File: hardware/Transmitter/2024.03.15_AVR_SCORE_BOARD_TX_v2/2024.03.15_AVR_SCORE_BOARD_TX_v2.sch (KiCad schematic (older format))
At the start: 44 parts, among them J1 Conn_01x10, J2 Conn_01x10, J3 Conn_01x05, Q1 BC817, SW1 SW_D1S+, SW10 D2S-, SW11 D2P+, SW12 D2P-, SW2 D1S-, SW3 SW_D1P+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

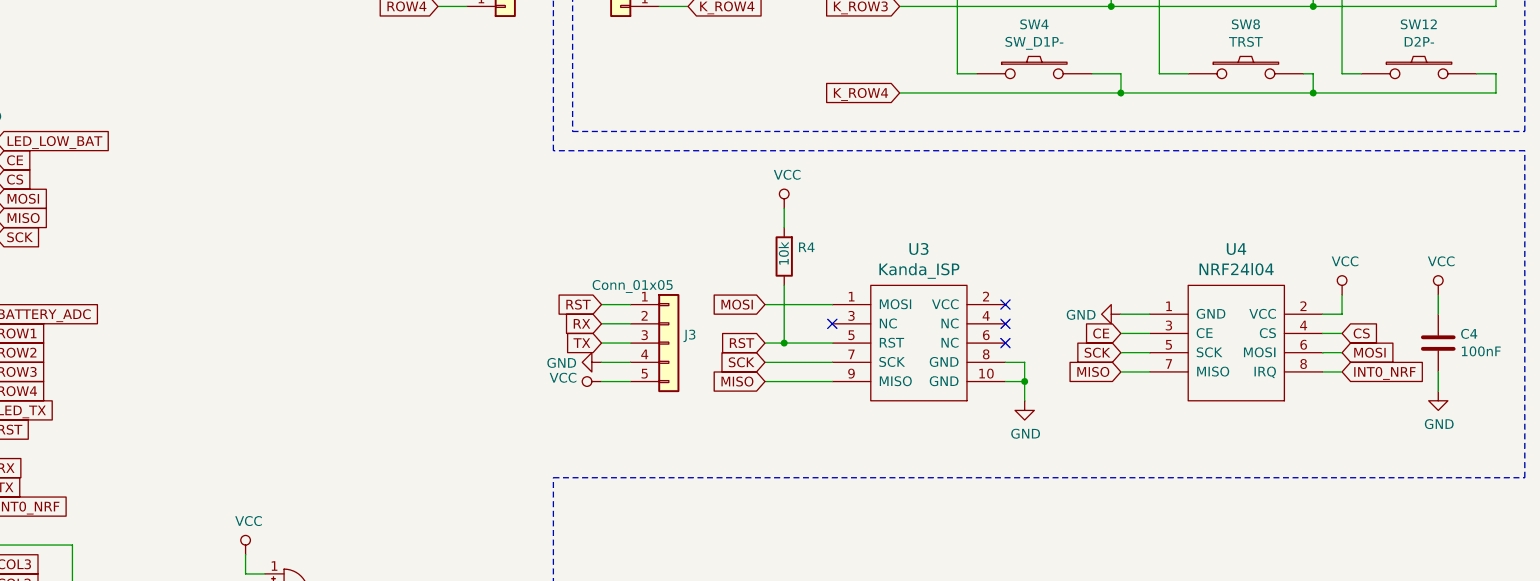
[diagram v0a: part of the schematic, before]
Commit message: Added LP2980 voltage regulator for NRF24L01
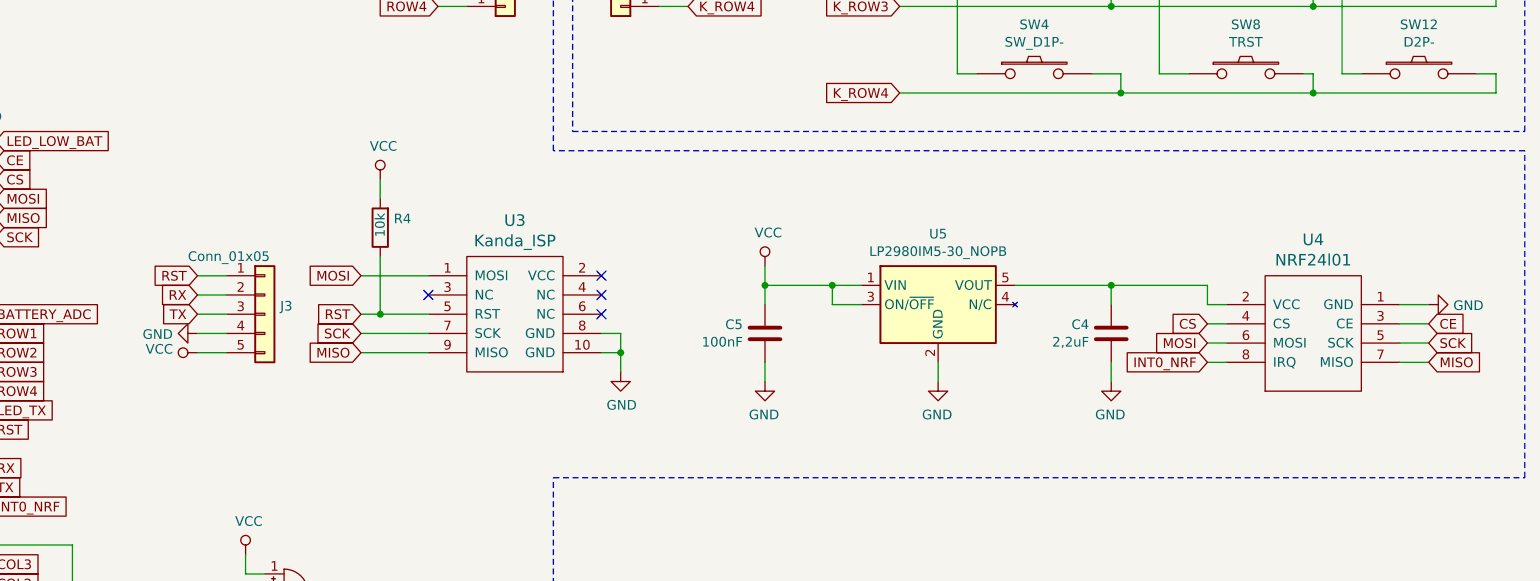
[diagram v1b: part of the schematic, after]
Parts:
- removed U4: NRF24l04, Moje:NRF24l01, symbol Moje:NRF24l04
- added C5: 100nF, Capacitor_SMD:C_0805_2012Metric_Pad1.15x1.40mm_HandSolder, symbol Device:C
- added U4: NRF24l01, Moje:NRF24l01, symbol Moje:NRF24l01
- added U5: LP2980IM5-30_NOPB, Package_TO_SOT_SMD:SOT-23-5, symbol Moje:LP2980IM5-30_NOPB
- C4: value 100nF -> 2,2uF
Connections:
- net CE: now also U4.3 (CE)
- net CS: now also U4.4 (CS)
- net GND: now also C5.2, U4.1 (GND), U5.2 (GND)
- net INT0_NRF: now also U4.8 (IRQ)
- net MISO: now also U4.7 (MISO)
- net MOSI: now also U4.6 (MOSI)
- net SCK: now also U4.5 (SCK)
- net VCC: now also C5.1, U5.1 (VIN), U5.3 (ON/~OFF); no longer C4.1
- new net: C4.1, U4.2 (VCC), U5.5 (VOUT)
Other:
- moved on the sheet: C4, J3, R4, U3

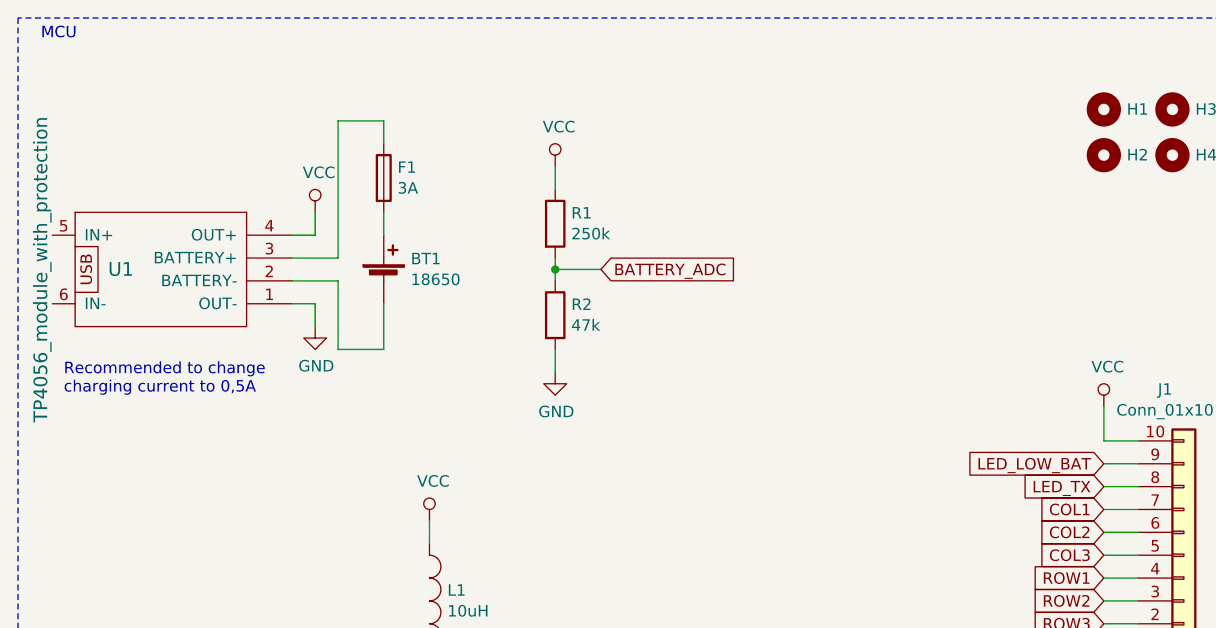
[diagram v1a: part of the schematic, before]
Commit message: Added USB_B for charging and moved old schematic
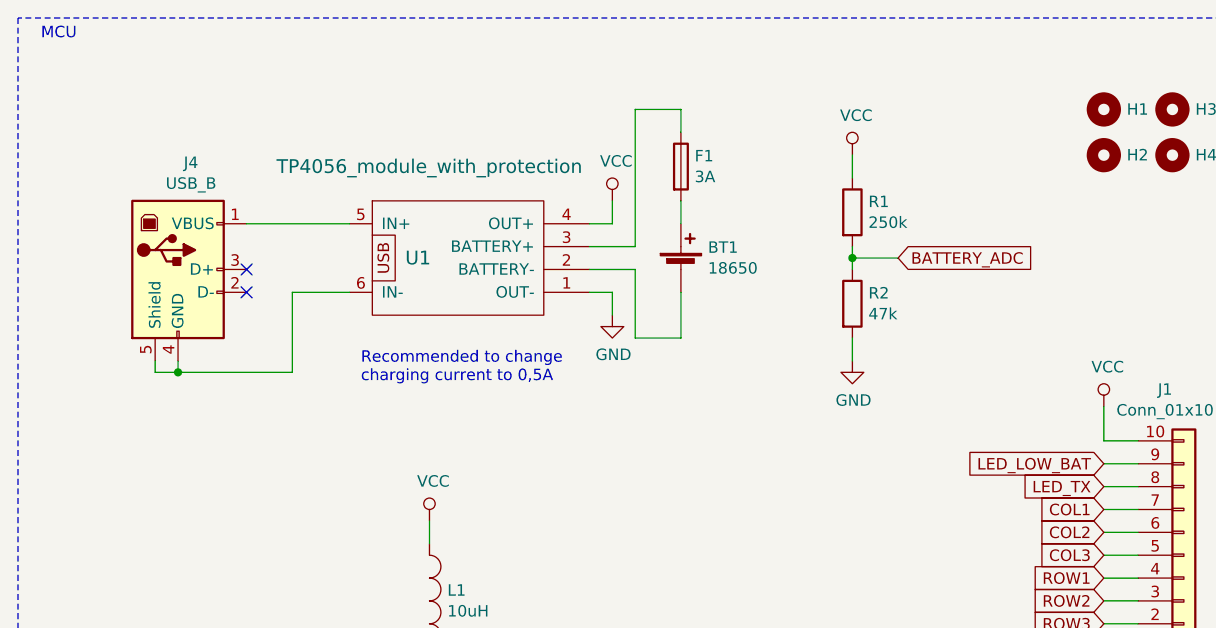
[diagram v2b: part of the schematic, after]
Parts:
- added J4: USB_B, Moje:USB_B, symbol Connector:USB_B
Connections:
- net at U1.5 (IN+): now also J4.1 (VBUS)
- net at U1.6 (IN-): now also J4.4 (GND), J4.5 (Shield)
- no-connect marks 7 -> 9
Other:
- moved on the sheet: BT1, F1, R1, R2, U1
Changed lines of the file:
@@
 L power:VCC #PWR0111
 U 1 1 660922B4
-P 2000 1450
-F 0 "#PWR0111" H 2000 1300 50  0001 C CNN
-F 1 "VCC" H 2017 1623 50  0000 C CNN
-F 2 "" H 2000 1450 50  0001 C CNN
-F 3 "" H 2000 1450 50  0001 C CNN
-	1    2000 1450
-	1    0    0    -1
-$EndComp
-Wire Wire Line
-	2000 1450 2000 1550
-Wire Wire Line
-	2000 1550 1900 1550
+P 3300 1400
+F 0 "#PWR0111" H 3300 1250 50  0001 C CNN
+F 1 "VCC" H 3317 1573 50  0000 C CNN
+F 2 "" H 3300 1400 50  0001 C CNN
+F 3 "" H 3300 1400 50  0001 C CNN
+	1    3300 1400
+	1    0    0    -1
+$EndComp
+Wire Wire Line
+	3300 1400 3300 1500
+Wire Wire Line
+	3300 1500 3200 1500
 $Comp
 L power:GND #PWR0112
 U 1 1 66096090
-P 2000 1950
-F 0 "#PWR0112" H 2000 1700 50  0001 C CNN
-F 1 "GND" H 2005 1777 50  0000 C CNN
-F 2 "" H 2000 1950 50  0001 C CNN
-F 3 "" H 2000 1950 50  0001 C CNN
-	1    2000 1950
-	1    0    0    -1
-$EndComp
-Wire Wire Line
-	2000 1950 2000 1850
+P 3300 1900
+F 0 "#PWR0112" H 3300 1650 50  0001 C CNN
+F 1 "GND" H 3305 1727 50  0000 C CNN
+F 2 "" H 3300 1900 50  0001 C CNN
+F 3 "" H 3300 1900 50  0001 C CNN
+	1    3300 1900
+	1    0    0    -1
+$EndComp
+Wire Wire Line
+	3300 1900 3300 1800
 $Comp
 L Device:R R1
 U 1 1 66099F55
-P 3050 1500
-F 0 "R1" H 3120 1546 50  0000 L CNN
-F 1 "250k" H 3120 1455 50  0000 L CNN
-F 2 "Moje:R_MY_DIN0204_L3.6mm_D1.6mm_P7.62mm" V 2980 1500 50  0001 C CNN
-F 3 "~" H 3050 1500 50  0001 C CNN
-	1    3050 1500
+P 4350 1450
+F 0 "R1" H 4420 1496 50  0000 L CNN
+F 1 "250k" H 4420 1405 50  0000 L CNN
+F 2 "Moje:R_MY_DIN0204_L3.6mm_D1.6mm_P7.62mm" V 4280 1450 50  0001 C CNN
+F 3 "~" H 4350 1450 50  0001 C CNN
+	1    4350 1450
 	1    0    0    -1
 $EndComp
@@
 L Device:R R2
 U 1 1 6609A28A
-P 3050 1900
-F 0 "R2" H 3120 1946 50  0000 L CNN
-F 1 "47k" H 3120 1855 50  0000 L CNN
-F 2 "Moje:R_MY_DIN0204_L3.6mm_D1.6mm_P7.62mm" V 2980 1900 50  0001 C CNN
-F 3 "~" H 3050 1900 50  0001 C CNN
-	1    3050 1900
-	1    0    0    -1
-$EndComp
-Wire Wire Line
-	3050 1650 3050 1700
+P 4350 1850
+F 0 "R2" H 4420 1896 50  0000 L CNN
+F 1 "47k" H 4420 1805 50  0000 L CNN
+F 2 "Moje:R_MY_DIN0204_L3.6mm_D1.6mm_P7.62mm" V 4280 1850 50  0001 C CNN
+F 3 "~" H 4350 1850 50  0001 C CNN
+	1    4350 1850
+	1    0    0    -1
+$EndComp
+Wire Wire Line
+	4350 1600 4350 1650
 $Comp
 L power:VCC #PWR0113
 U 1 1 660A22CA
-P 3050 1250
-F 0 "#PWR0113" H 3050 1100 50  0001 C CNN
-F 1 "VCC" H 3067 1423 50  0000 C CNN
-F 2 "" H 3050 1250 50  0001 C CNN
-F 3 "" H 3050 1250 50  0001 C CNN
-	1    3050 1250
-	1    0    0    -1
-$EndComp
-Wire Wire Line
-	3050 1250 3050 1350
+P 4350 1200
+F 0 "#PWR0113" H 4350 1050 50  0001 C CNN
+F 1 "VCC" H 4367 1373 50  0000 C CNN
+F 2 "" H 4350 1200 50  0001 C CNN
+F 3 "" H 4350 1200 50  0001 C CNN
+	1    4350 1200
+	1    0    0    -1
+$EndComp
+Wire Wire Line
+	4350 1200 4350 1300
 $Comp
 L power:GND #PWR0114
 U 1 1 660A6387
-P 3050 2150
-F 0 "#PWR0114" H 3050 1900 50  0001 C CNN
-F 1 "GND" H 3055 1977 50  0000 C CNN
-F 2 "" H 3050 2150 50  0001 C CNN
-F 3 "" H 3050 2150 50  0001 C CNN
-	1    3050 2150
-	1    0    0    -1
-$EndComp
-Wire Wire Line
-	3050 2150 3050 2050
-Text GLabel 3250 1700 2    50   Input ~ 0
+P 4350 2100
+F 0 "#PWR0114" H 4350 1850 50  0001 C CNN
+F 1 "GND" H 4355 1927 50  0000 C CNN
+F 2 "" H 4350 2100 50  0001 C CNN
+F 3 "" H 4350 2100 50  0001 C CNN
+	1    4350 2100
+	1    0    0    -1
+$EndComp
+Wire Wire Line
+	4350 2100 4350 2000
+Text GLabel 4550 1650 2    50   Input ~ 0
 BATTERY_ADC
 Wire Wire Line
-	3250 1700 3050 1700
-Connection ~ 3050 1700
-Wire Wire Line
-	3050 1700 3050 1750
+	4550 1650 4350 1650
+Connection ~ 4350 1650
+Wire Wire Line
+	4350 1650 4350 1700
 $Comp
 L Connector_Generic:Conn_01x05 J3
@@
 L Moje:TP4056_module_with_protection U1
 U 1 1 6623C86A
-P 1350 1700
-F 0 "U1" H 1150 1700 60  0000 C CNN
-F 1 "TP4056_module_with_protection" V 800 1700 60  0000 C CNN
-F 2 "Moje:TP4056-18650" H 1300 1700 60  0001 C CNN
-F 3 "" H 1300 1700 60  0001 C CNN
-	1    1350 1700
+P 2650 1650
+F 0 "U1" H 2450 1650 60  0000 C CNN
+F 1 "TP4056_module_with_protection" H 2500 2050 60  0000 C CNN
+F 2 "Moje:TP4056-18650" H 2600 1650 60  0001 C CNN
+F 3 "" H 2600 1650 60  0001 C CNN
+	1    2650 1650
 	1    0    0    -1
 $EndComp
@@
 L Device:Battery_Cell BT1
 U 1 1 6623E50B
-P 2300 1750
-F 0 "BT1" H 2418 1846 50  0000 L CNN
-F 1 "18650" H 2418 1755 50  0000 L CNN
-F 2 "Battery:BatteryHolder_MPD_BH-18650-PC2" V 2300 1810 50  0001 C CNN
-F 3 "~" V 2300 1810 50  0001 C CNN
-	1    2300 1750
-	1    0    0    -1
-$EndComp
-Wire Wire Line
-	1900 1850 2000 1850
+P 3600 1700
+F 0 "BT1" H 3718 1796 50  0000 L CNN
+F 1 "18650" H 3718 1705 50  0000 L CNN
+F 2 "Battery:BatteryHolder_MPD_BH-18650-PC2" V 3600 1760 50  0001 C CNN
+F 3 "~" V 3600 1760 50  0001 C CNN
+	1    3600 1700
+	1    0    0    -1
+$EndComp
+Wire Wire Line
+	3200 1800 3300 1800
 $Comp
 L Device:Fuse F1
 U 1 1 662AAE57
-P 2300 1300
-F 0 "F1" H 2360 1346 50  0000 L CNN
-F 1 "3A" H 2360 1255 50  0000 L CNN
-F 2 "Fuse:Fuse_0805_2012Metric_Pad1.15x1.40mm_HandSolder" V 2230 1300 50  0001 C CNN
-F 3 "~" H 2300 1300 50  0001 C CNN
-	1    2300 1300
-	1    0    0    -1
-$EndComp
-Wire Wire Line
-	2300 1450 2300 1550
-Wire Wire Line
-	2300 1150 2300 1050
-Wire Wire Line
-	2300 1050 2100 1050
-Wire Wire Line
-	2100 1050 2100 1650
-Wire Wire Line
-	2100 1650 1900 1650
-Wire Wire Line
-	1900 1750 2100 1750
-Wire Wire Line
-	2100 1750 2100 2050
-Wire Wire Line
-	2100 2050 2300 2050
-Wire Wire Line
-	2300 2050 2300 1850
-Text Notes 900  2250 0    50   ~ 0
+P 3600 1250
+F 0 "F1" H 3660 1296 50  0000 L CNN
+F 1 "3A" H 3660 1205 50  0000 L CNN
+F 2 "Fuse:Fuse_0805_2012Metric_Pad1.15x1.40mm_HandSolder" V 3530 1250 50  0001 C CNN
+F 3 "~" H 3600 1250 50  0001 C CNN
+	1    3600 1250
+	1    0    0    -1
+$EndComp
+Wire Wire Line
+	3600 1400 3600 1500
+Wire Wire Line
+	3600 1100 3600 1000
+Wire Wire Line
+	3600 1000 3400 1000
+Wire Wire Line
+	3400 1000 3400 1600
+Wire Wire Line
+	3400 1600 3200 1600
+Wire Wire Line
+	3200 1700 3400 1700
+Wire Wire Line
+	3400 1700 3400 2000
+Wire Wire Line
+	3400 2000 3600 2000
+Wire Wire Line
+	3600 2000 3600 1800
+Text Notes 2200 2200 0    50   ~ 0
 Recommended to change \ncharging current to 0,5A
 $Comp
@@
 	1    0    0    1
 $EndComp
+$Comp
+L Connector:USB_B J4
+U 1 1 671F996B
+P 1400 1700
+F 0 "J4" H 1457 2167 50  0000 C CNN
+F 1 "USB_B" H 1457 2076 50  0000 C CNN
+F 2 "Moje:USB_B" H 1550 1650 50  0001 C CNN
+F 3 " ~" H 1550 1650 50  0001 C CNN
+	1    1400 1700
+	1    0    0    -1
+$EndComp
+Wire Wire Line
+	1700 1500 2150 1500
+NoConn ~ 1700 1700
+NoConn ~ 1700 1800
+Wire Wire Line
+	2150 1800 1900 1800
+Wire Wire Line
+	1900 1800 1900 2150
+Wire Wire Line
+	1900 2150 1400 2150
+Wire Wire Line
+	1300 2150 1300 2100
+Wire Wire Line
+	1400 2100 1400 2150
+Connection ~ 1400 2150
+Wire Wire Line
+	1400 2150 1300 2150
 $EndSCHEMATC

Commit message: Update label
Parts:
- SW6: value SW_H- -> SW_M+
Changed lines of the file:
@@
 P 9650 2650
 F 0 "SW6" H 9650 2905 50  0000 C CNN
-F 1 "SW_H-" H 9650 2814 50  0000 C CNN
+F 1 "SW_M+" H 9650 2814 50  0000 C CNN
 F 2 "Moje:SW_SMALL(6X6)" H 9650 2650 50  0001 C CNN
 F 3 "" H 9650 2650 50  0000 C CNN
